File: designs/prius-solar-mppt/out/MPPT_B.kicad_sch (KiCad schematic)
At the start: 79 parts, among them J201 1757242, Q201 IAUC100N10, Q202 MMBTA42, Q203 IAUC100N10, Q204 IAUC100N10, Q205 IAUC100N10, Q206 IAUC100N10, U201 LM74700-Q1, U202 INA186A2QDBVRQ1, U203 LM5176QPWPRQ1, U204 TLV9001-Q1

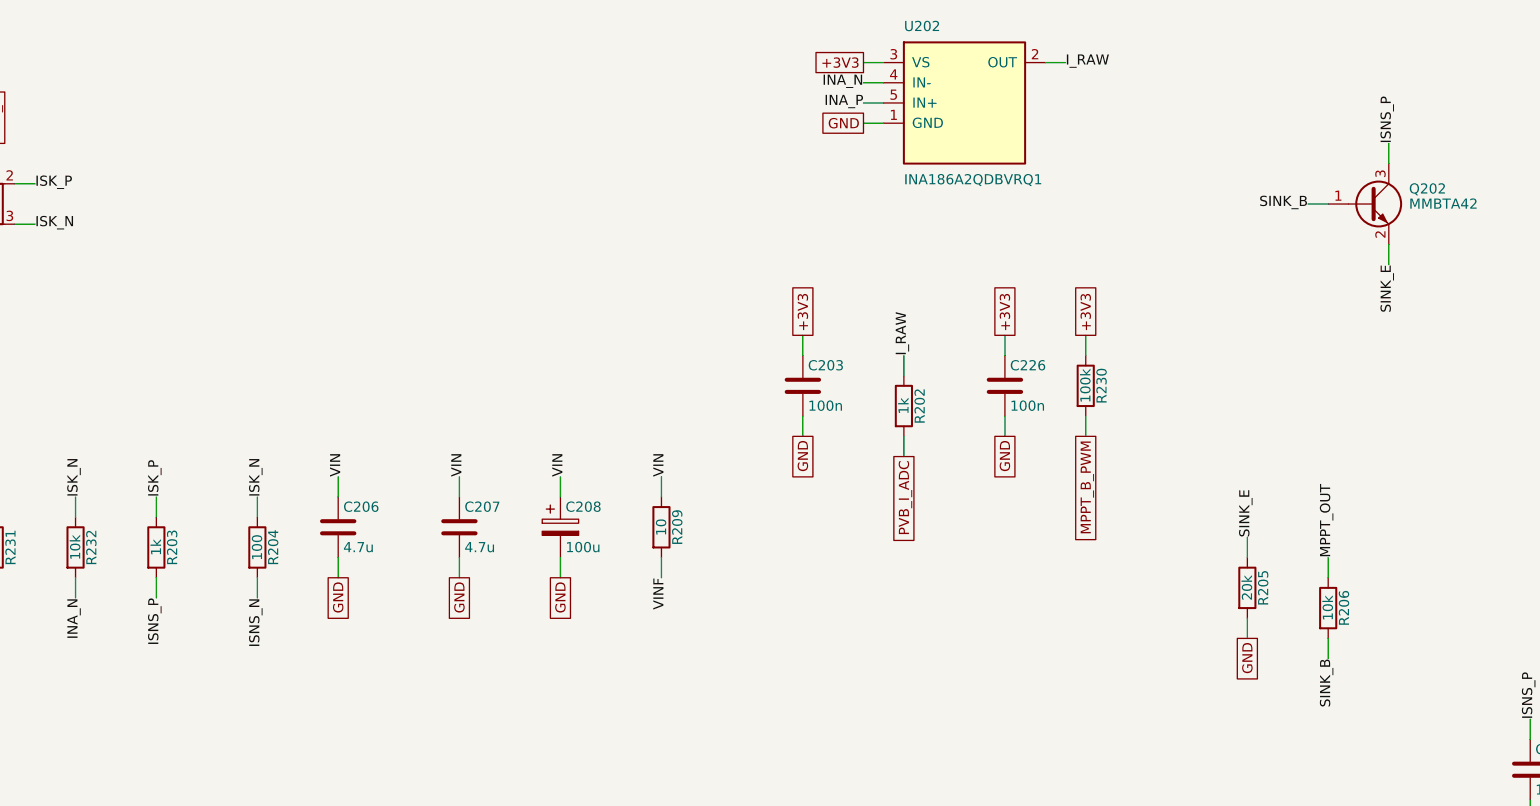
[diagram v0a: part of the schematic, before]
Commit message: designs/prius-solar-mppt: rework for the 2017 Prius Prime (Li-ion), charging car on and off
User decisions (2026-10-23): it is a Prius Prime with the Li-ion pack; it must charge
with the car on or off, be smart, and be weak enough that the pack cannot get into
trouble (stop by 80 %, voltage clamp, temperature compensation).

- Pack: 95 cells in series; no Prius pack is split while off (relays sit on the two pack
  cables; the service plug splits it only when pulled), so one tap pair on the cell side
  of the system main relays, fused on both poles, reaches the whole pack.
- Weak by construction: charge current capped at 0.30 A (>= 2 sun-days from 80 % to 100 %
  with firmware dead), analog CV/CC limiter on its own reference, latching overcurrent
  and overvoltage trips, 1:22 isolating DC transformer stage, 600 V relays, pack-sense
  core in the harness, event log, CAN transmit gated by ignition.
- Toyota's 180 W Prius PHV solar roof ("pump charging" through a buffer battery and the
  car's battery ECU) documented as the reference; this board does that ECU's job itself.
- Encoded in kaesynth: main (470 parts) and battery-end (15) boards, both netlists
  identical to the IR; 0 errors, 32 waived. The checks caught two v0.1 errors: an
  inverted UVLO (the stage never turned off) and the MPPT current sink on the wrong input.
- Blocking: roof measurement, junction-block tap location, installer/legality, roof
  fixing, and Q-10.

Co-Authored-By: Claude Opus 5.5 <noreply@anthropic.com>
Claude-Session: https://claude.ai/code/session_01VFJn9VbX8h27kf4LpLwEtn
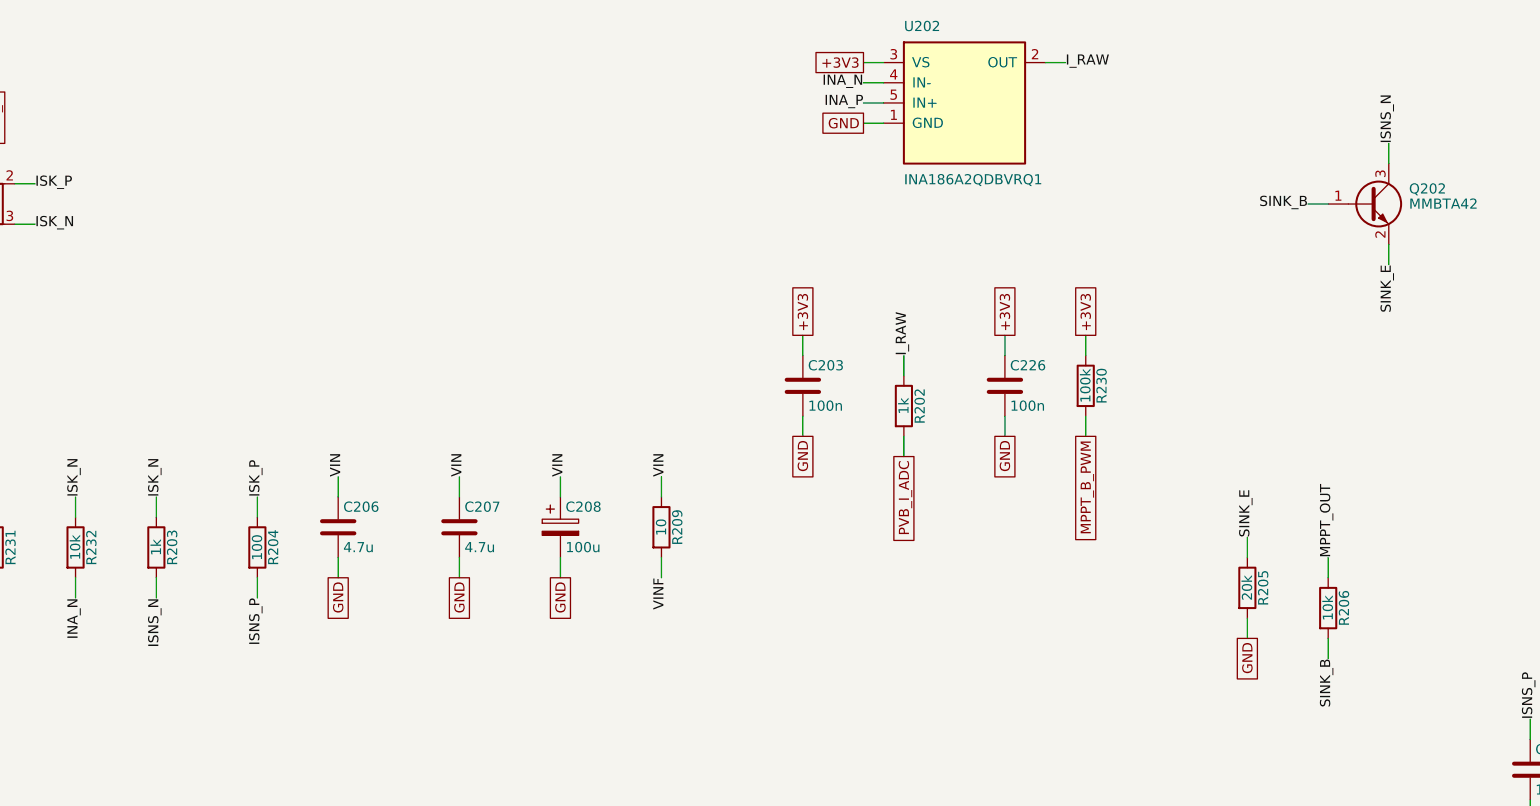
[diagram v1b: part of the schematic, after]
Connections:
- net ISK_N: now also R203.1; no longer R204.1
- net ISK_P: now also R204.1; no longer R203.1
- net ISNS_N: now also Q202.3 (C), R203.2; no longer R204.2
- net ISNS_P: now also R204.2; no longer Q202.3 (C), R203.2
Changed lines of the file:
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@@
 		)
 	)
-	(label "ISK_P"
+	(label "ISK_N"
 		(at 180.34 85.09 90)
 		(fields_autoplaced yes)
@@
 		)
 	)
-	(label "ISNS_P"
+	(label "ISNS_N"
 		(at 180.34 97.79 270)
 		(fields_autoplaced yes)
@@
 		)
 	)
-	(label "ISK_N"
+	(label "ISK_P"
 		(at 193.04 85.09 90)
 		(fields_autoplaced yes)
@@
 		)
 	)
-	(label "ISNS_N"
+	(label "ISNS_P"
 		(at 193.04 97.79 270)
 		(fields_autoplaced yes)
@@
 		)
 	)
-	(label "ISNS_P"
+	(label "ISNS_N"
 		(at 335.28 40.64 90)
 		(fields_autoplaced yes)

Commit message: designs/prius-solar-mppt: v0.3, fix the independent review's blockers and majors
- B1: CHASSIS domain with reinforced DC barriers to HV and PACK (10/8 mm), HV/PACK edge
  clearance 10 mm, mounting holes fixed with 13 mm keep-outs; thermal pedestal under LV
  parts only.
- B2: no primary source for the Prime's full-charge cell voltage was found (blocking
  Q-13); hardware clamp set below a 4.00 V/cell floor (L3 3.927 V, worst 3.963 V; L2
  3.836 V; L1 3.79 V) with DNP trim to raise later; until then charging may stop near
  55-65 % SOC.
- Majors: sink clamp + burst disable + PV-node trip and TVS against LM5176 reverse power;
  20 MHz AEC-Q200 crystal for CAN (listen-only start); parked insulation monitoring via a
  110 M bridge (also detects a welded relay); open-sensor-safe hardware OT; CAGE CLAMP HV
  terminals with a lid-switch HVIL; DCX on-time and 17.6 A primary overcurrent latches;
  supercap-held latch that clears overnight.
- Build: 0 errors, ERC clean, system and both board netlists identical; 9 waivers (17
  findings, was 32).

Co-Authored-By: Claude Opus 5.5 <noreply@anthropic.com>
Claude-Session: https://claude.ai/code/session_01VFJn9VbX8h27kf4LpLwEtn
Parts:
- added C230: 10n, Capacitor_SMD:C_0603_1608Metric, symbol Device:C
- added D206, D208: BAT46WJ, Diode_SMD:D_SOD-323F, symbol Diode:BAT46
- added D207: TPSMB43A, Diode_SMD:D_SMB, symbol Device:D_Zener
- added R233: 160k, Resistor_SMD:R_0603_1608Metric, symbol Device:R
- added R234: 10k, Resistor_SMD:R_0603_1608Metric, symbol Device:R
- R205: value 20k -> 75k; MPN ERJ-3EKF2002V -> ERJ-3EKF7502V
- R208: value 137k -> 162k; MPN ERJ-3EKF1373V -> ERJ-3EKF1623V
- R214: value 442k -> 432k; MPN TNPW1206442KBEEA -> TNPW1206432KBEEA
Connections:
- net EN: now also D206.2 (A), D208.2 (A)
- net GND: now also C230.2, D207.2 (A), R234.2
- net PVB_P: now also D207.1 (K), R233.1
- new net BURST_N: D206.1 (K)
- new net PVB_OVS: C230.1, R233.2, R234.1
- new net PVB_OV_N: D208.1 (K)
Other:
- moved on the sheet: C203, C204, C205, C206, C207, C208, C209, C210, C211, C212, C213, C214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
